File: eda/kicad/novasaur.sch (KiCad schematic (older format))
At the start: 29 parts, among them U1 74F86, U10 74F574, U11 74F574, U12 PAL16R4, U2 74F32, U3 74F11, U4 74F139, U5 74F139, U6 74F157, U7 74F175, U8 74F574, U9 74F138, X1 33M

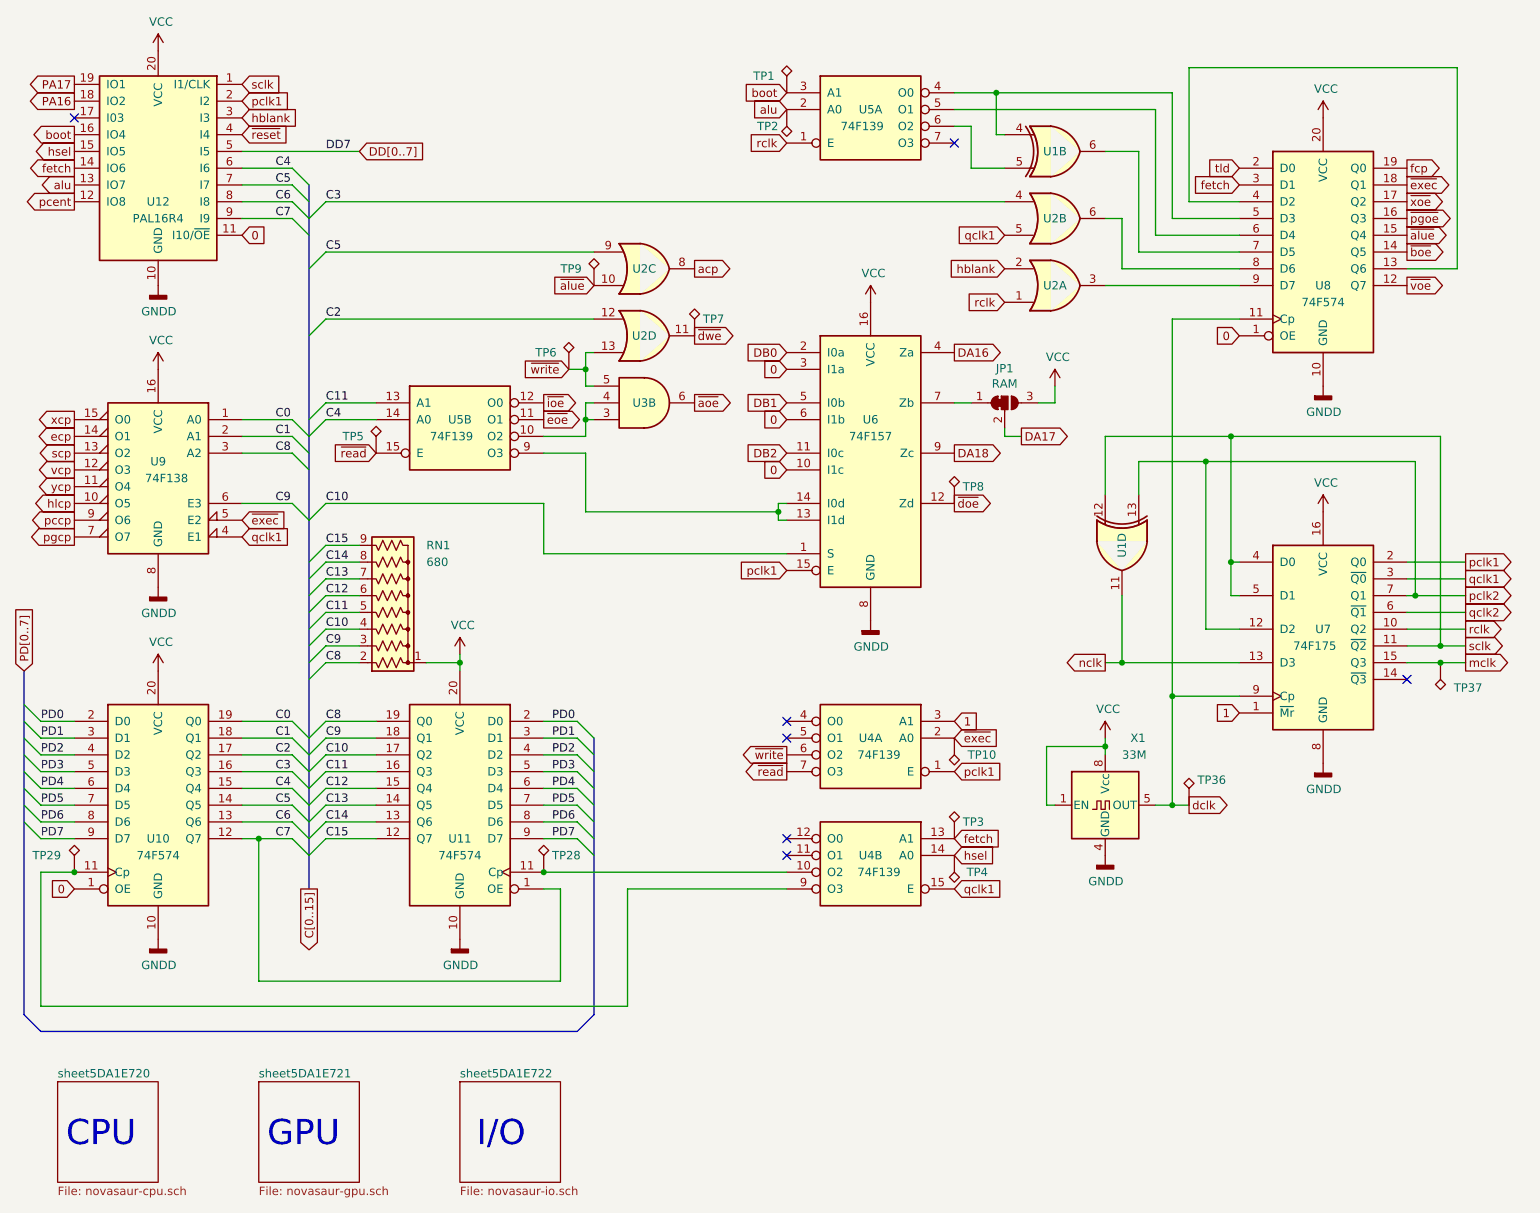
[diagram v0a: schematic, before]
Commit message: add TVS diode ESD protection
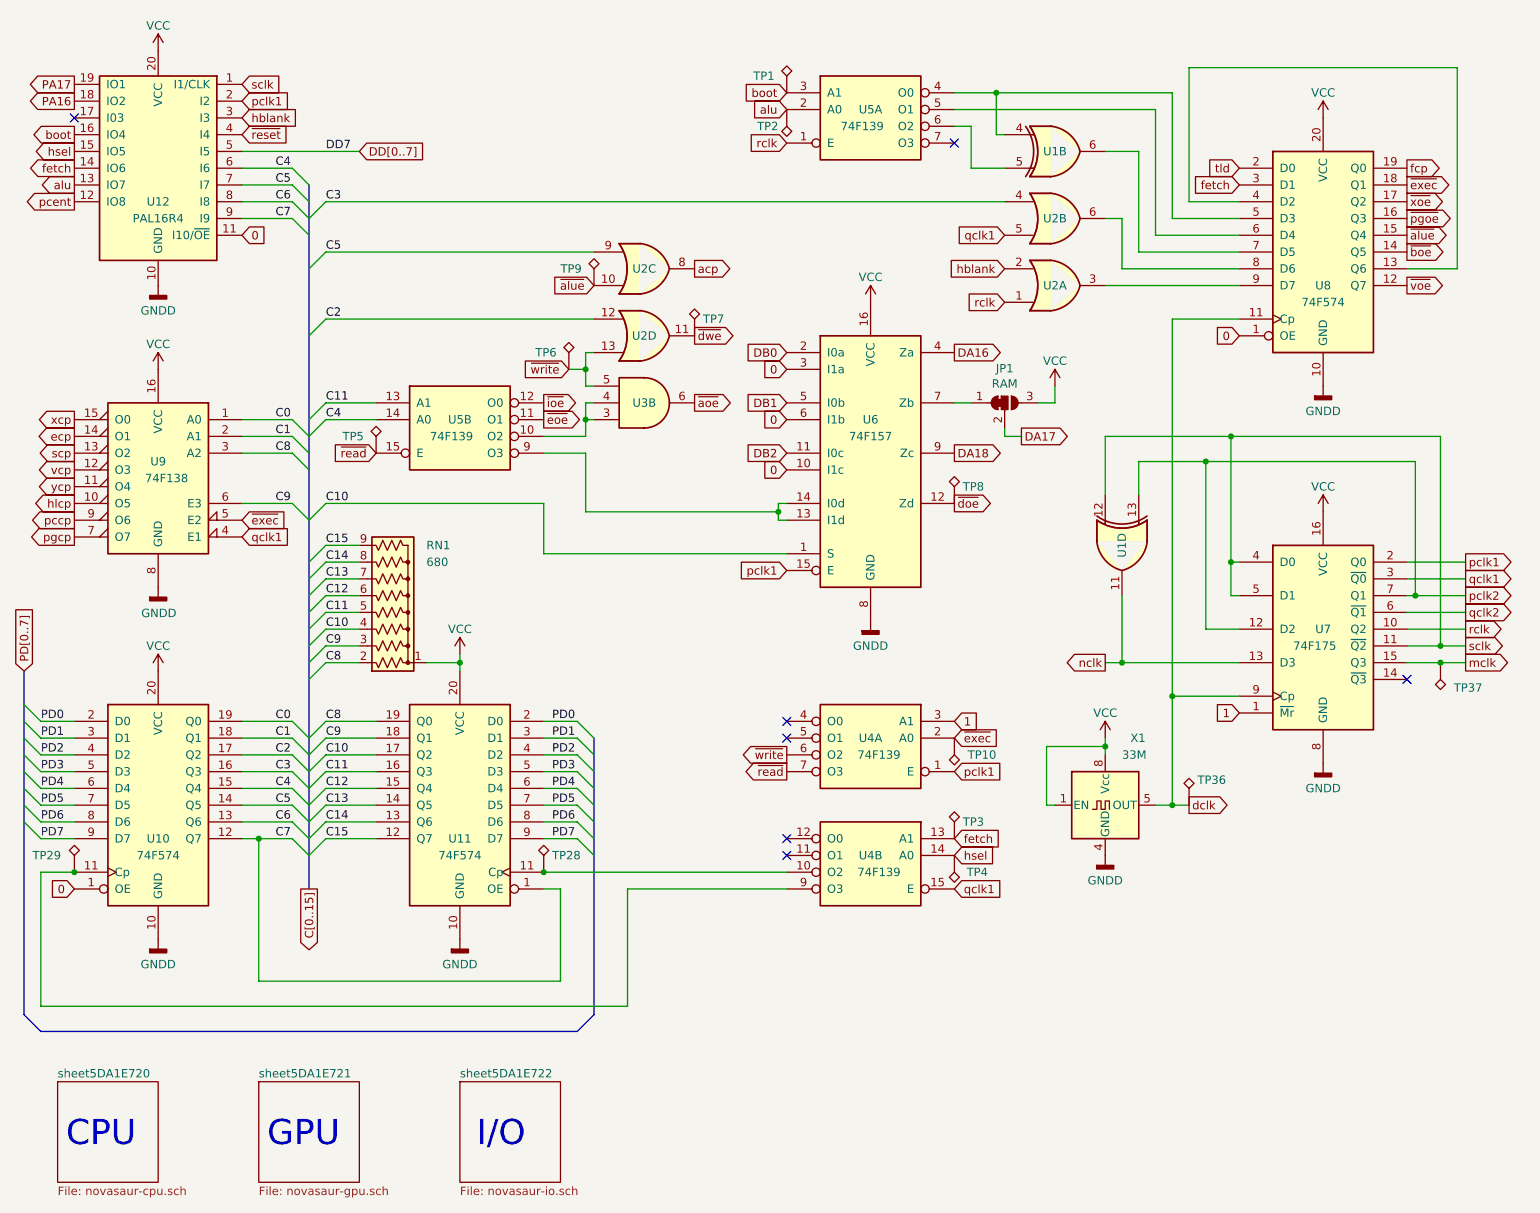
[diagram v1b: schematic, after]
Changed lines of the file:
@@
 Sheet 1 4
 Title "Novasaur Retrocomputer"
-Date "2021-06-06"
-Rev "1.9"
+Date "2021-07-10"
+Rev "1.10"
 Comp ""
 Comment1 "(c) Solid State Machines 2021"
@@
 AR Path="/5DA1E953" Ref="#PWR0114"  Part="1"
 F 0 "#PWR0114" H 1850 6050 50  0001 C CNN
-F 1 "GNDD" H 1854 6145 50  0000 C CNN
+F 1 "GNDD" H 1850 6150 50  0000 C CNN
 F 2 "" H 1850 6300 50  0001 C CNN
 F 3 "" H 1850 6300 50  0001 C CNN
@@
 AR Path="/5DA1E817" Ref="#PWR0110"  Part="1"
 F 0 "#PWR0110" H 1850 2150 50  0001 C CNN
-F 1 "GNDD" H 1854 2245 50  0000 C CNN
+F 1 "GNDD" H 1850 2250 50  0000 C CNN
 F 2 "" H 1850 2400 50  0001 C CNN
 F 3 "" H 1850 2400 50  0001 C CNN
@@
 AR Path="/5DA1E7E3" Ref="#PWR0107"  Part="1"
 F 0 "#PWR0107" H 3650 6050 50  0001 C CNN
-F 1 "GNDD" H 3654 6145 50  0000 C CNN
+F 1 "GNDD" H 3650 6150 50  0000 C CNN
 F 2 "" H 3650 6300 50  0001 C CNN
 F 3 "" H 3650 6300 50  0001 C CNN
@@
 AR Path="/5DA1E785" Ref="#PWR0105"  Part="1"
 F 0 "#PWR0105" H 1850 4550 50  0001 C CNN
-F 1 "VCC" H 1867 4873 50  0000 C CNN
+F 1 "VCC" H 1850 4850 50  0000 C CNN
 F 2 "" H 1850 4700 50  0001 C CNN
 F 3 "" H 1850 4700 50  0001 C CNN
@@
 AR Path="/5DA1E756" Ref="#PWR0104"  Part="1"
 F 0 "#PWR0104" H 1850 2750 50  0001 C CNN
-F 1 "VCC" H 1867 3073 50  0000 C CNN
+F 1 "VCC" H 1850 3050 50  0000 C CNN
 F 2 "" H 1850 2900 50  0001 C CNN
 F 3 "" H 1850 2900 50  0001 C CNN
@@
 AR Path="/5DA1E7F9" Ref="#PWR0108"  Part="1"
 F 0 "#PWR0108" H 3650 4450 50  0001 C CNN
-F 1 "VCC" H 3667 4773 50  0000 C CNN
+F 1 "VCC" H 3650 4750 50  0000 C CNN
 F 2 "" H 3650 4600 50  0001 C CNN
 F 3 "" H 3650 4600 50  0001 C CNN
@@
 AR Path="/5EAB4390" Ref="#PWR0101"  Part="1"
 F 0 "#PWR0101" H 8800 2750 50  0001 C CNN
-F 1 "GNDD" H 8804 2845 50  0000 C CNN
+F 1 "GNDD" H 8800 2850 50  0000 C CNN
 F 2 "" H 8800 3000 50  0001 C CNN
 F 3 "" H 8800 3000 50  0001 C CNN
@@
 AR Path="/5EAB4396" Ref="#PWR0106"  Part="1"
 F 0 "#PWR0106" H 8800 1250 50  0001 C CNN
-F 1 "VCC" H 8817 1573 50  0000 C CNN
+F 1 "VCC" H 8800 1550 50  0000 C CNN
 F 2 "" H 8800 1400 50  0001 C CNN
 F 3 "" H 8800 1400 50  0001 C CNN
@@
 AR Path="/5DE9082F" Ref="#PWR0113"  Part="1"
 F 0 "#PWR0113" H 1850 850 50  0001 C CNN
-F 1 "VCC" H 1867 1173 50  0000 C CNN
+F 1 "VCC" H 1850 1150 50  0000 C CNN
 F 2 "" H 1850 1000 50  0001 C CNN
 F 3 "" H 1850 1000 50  0001 C CNN
@@
 AR Path="/5E57D7F8" Ref="#PWR0192"  Part="1"
 F 0 "#PWR0192" H 6100 2350 50  0001 C CNN
-F 1 "VCC" H 6117 2673 50  0000 C CNN
+F 1 "VCC" H 6100 2650 50  0000 C CNN
 F 2 "" H 6100 2500 50  0001 C CNN
 F 3 "" H 6100 2500 50  0001 C CNN
@@
 AR Path="/5D9CBE89" Ref="#PWR0112"  Part="1"
 F 0 "#PWR0112" H 7500 5550 50  0001 C CNN
-F 1 "GNDD" H 7504 5645 50  0000 C CNN
+F 1 "GNDD" H 7500 5650 50  0000 C CNN
 F 2 "" H 7500 5800 50  0001 C CNN
 F 3 "" H 7500 5800 50  0001 C CNN
@@
 AR Path="/5DAA5CD8/5D9DED2A" Ref="#PWR?"  Part="1"
 F 0 "#PWR0191" H 7500 4950 50  0001 C CNN
-F 1 "VCC" H 7517 5273 50  0000 C CNN
+F 1 "VCC" H 7500 5250 50  0000 C CNN
 F 2 "" H 7500 5100 50  0001 C CNN
 F 3 "" H 7500 5100 50  0001 C CNN
@@
 AR Path="/5DEA197D" Ref="#PWR0103"  Part="1"
 F 0 "#PWR0103" H 8800 5000 50  0001 C CNN
-F 1 "GNDD" H 8804 5095 50  0000 C CNN
+F 1 "GNDD" H 8800 5100 50  0000 C CNN
 F 2 "" H 8800 5250 50  0001 C CNN
 F 3 "" H 8800 5250 50  0001 C CNN
@@
 AR Path="/5DA5D9DA" Ref="#PWR0102"  Part="1"
 F 0 "#PWR0102" H 8800 3600 50  0001 C CNN
-F 1 "VCC" H 8817 3923 50  0000 C CNN
+F 1 "VCC" H 8800 3900 50  0000 C CNN
 F 2 "" H 8800 3750 50  0001 C CNN
 F 3 "" H 8800 3750 50  0001 C CNN
@@
 AR Path="/5E58D7F4" Ref="#PWR0193"  Part="1"
 F 0 "#PWR0193" H 6100 4150 50  0001 C CNN
-F 1 "GNDD" H 6104 4245 50  0000 C CNN
+F 1 "GNDD" H 6100 4250 50  0000 C CNN
 F 2 "" H 6100 4400 50  0001 C CNN
 F 3 "" H 6100 4400 50  0001 C CNN
@@
 AR Path="/5EAF98E7" Ref="#PWR0198"  Part="1"
 F 0 "#PWR0198" H 7200 2850 50  0001 C CNN
-F 1 "VCC" H 7217 3173 50  0000 C CNN
+F 1 "VCC" H 7200 3150 50  0000 C CNN
 F 2 "" H 7200 3000 50  0001 C CNN
 F 3 "" H 7200 3000 50  0001 C CNN

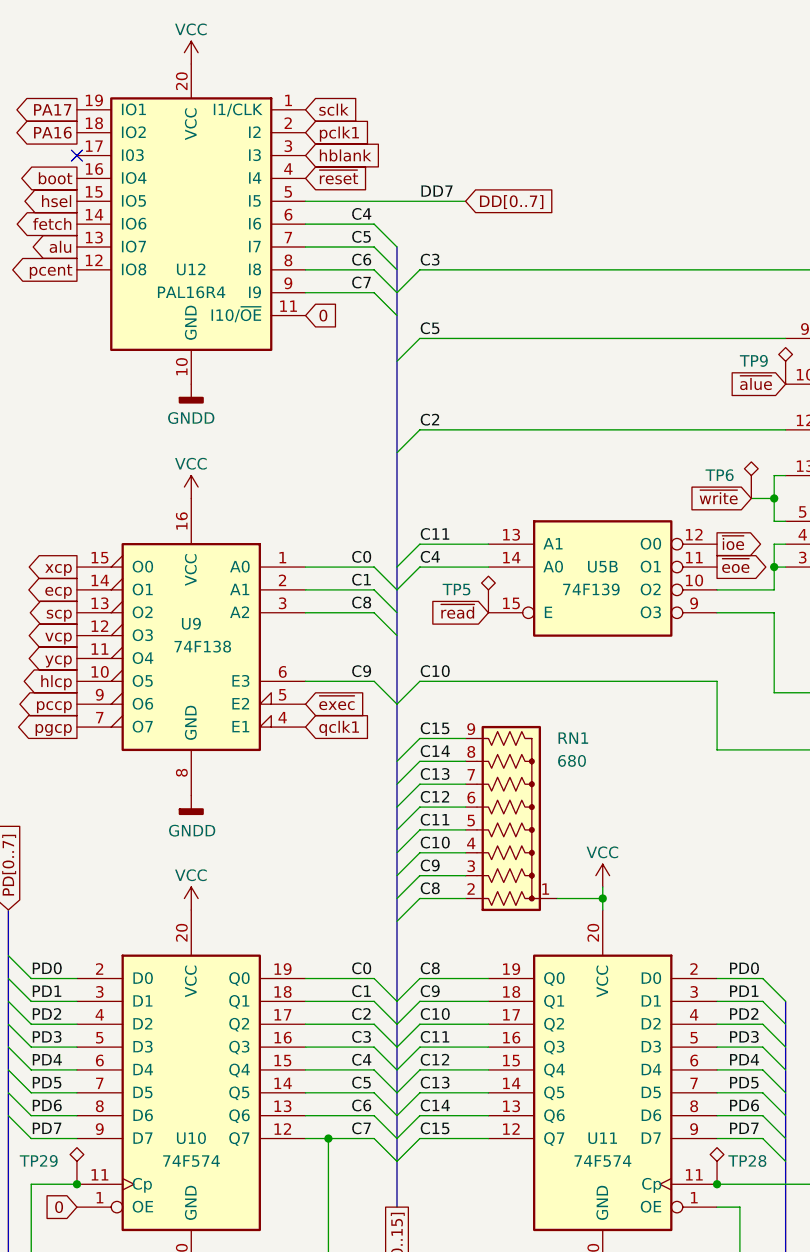
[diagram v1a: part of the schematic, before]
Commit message: remove 6v regulator go back to rev.1 do not collect 00
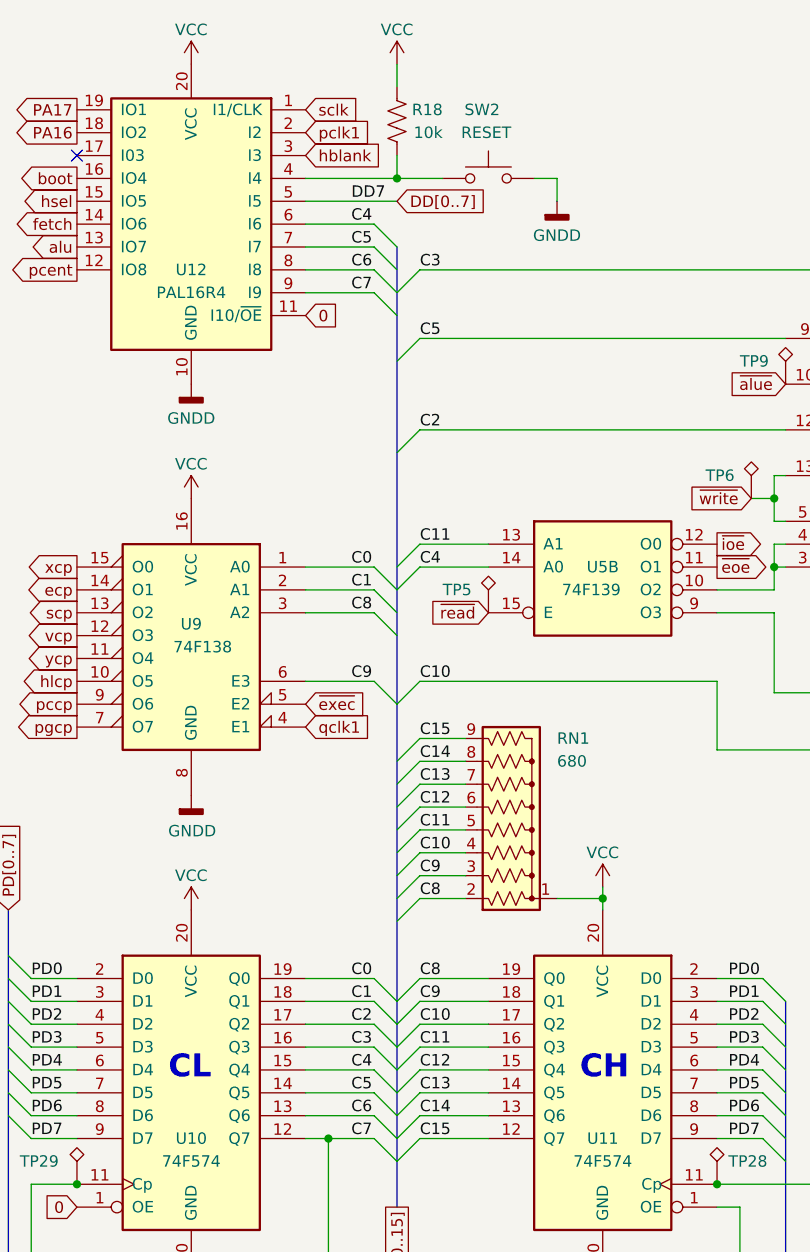
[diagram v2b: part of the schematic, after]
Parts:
- added R18: 10k, Resistor_THT:R_Axial_DIN0204_L3.6mm_D1.6mm_P7.62mm_Horizontal, symbol Device:R_US
- added SW2: RESET, Button_Switch_THT:SW_Tactile_SPST_Angled_PTS645Vx31-2LFS, symbol Switch:SW_Push
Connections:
- net GNDD: now also SW2.1
- net VCC: now also R18.2
- net ~reset: no longer names the net of U12.4 (I4)
- net ~reset: now also R18.1, SW2.2
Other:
- note added: "CH"
- note added: "CL"
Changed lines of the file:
@@
 Sheet 1 4
 Title "Novasaur Retrocomputer"
-Date "2021-07-10"
+Date "2021-08-01"
 Rev "1.10"
 Comp ""
@@
 	5600 5900 4150 5900
 Connection ~ 4150 5900
-Text GLabel 2350 1500 2    50   Input ~ 0
-~reset
 $Comp
 L Connector:TestPoint_Alt TP28
@@
 Wire Wire Line
 	9500 4650 9650 4650
-Wire Wire Line
-	2350 1600 3050 1600
-Text Label 2850 1600 0    50   ~ 0
+Text Label 2550 1600 0    50   ~ 0
 DD7
-Text GLabel 3050 1600 2    50   Input ~ 0
+Text GLabel 2750 1600 2    50   Input ~ 0
 DD[0..7]
 $Comp
@@
 Wire Wire Line
 	4150 4000 5600 4000
+Text Notes 1750 5450 0    100  ~ 20
+CL
+Text Notes 3550 5450 0    100  ~ 20
+CH
+$Comp
+L Device:R_US R?
+U 1 1 6116EADB
+P 2750 1250
+AR Path="/62D13D9D/6116EADB" Ref="R?"  Part="1"
+AR Path="/5DAA5CD8/5D9AFF37/6116EADB" Ref="R?"  Part="1"
+AR Path="/5DA1E9C0/6116EADB" Ref="R?"  Part="1"
+AR Path="/6116EADB" Ref="R18"  Part="1"
+F 0 "R18" H 2550 1200 50  0000 L CNN
+F 1 "10k" H 2550 1300 50  0000 L CNN
+F 2 "Resistor_THT:R_Axial_DIN0204_L3.6mm_D1.6mm_P7.62mm_Horizontal" V 2790 1240 50  0001 C CNN
+F 3 "~" H 2750 1250 50  0001 C CNN
+	1    2750 1250
+	-1   0    0    1
+$EndComp
+$Comp
+L Switch:SW_Push SW?
+U 1 1 6116EAE1
+P 3150 1500
+AR Path="/5DA1E9C0/6116EAE1" Ref="SW?"  Part="1"
+AR Path="/6116EAE1" Ref="SW2"  Part="1"
+F 0 "SW2" H 3100 1800 50  0000 L CNN
+F 1 "RESET" H 3050 1700 50  0000 L CNN
+F 2 "Button_Switch_THT:SW_Tactile_SPST_Angled_PTS645Vx31-2LFS" H 3150 1700 50  0001 C CNN
+F 3 "~" H 3150 1700 50  0001 C CNN
+	1    3150 1500
+	-1   0    0    -1
+$EndComp
+$Comp
+L power:VCC #PWR?
+U 1 1 611A0A05
+P 2750 1000
+AR Path="/5CDEEC9F/611A0A05" Ref="#PWR?"  Part="1"
+AR Path="/5DAA5CD8/611A0A05" Ref="#PWR?"  Part="1"
+AR Path="/611A0A05" Ref="#PWR0197"  Part="1"
+F 0 "#PWR0197" H 2750 850 50  0001 C CNN
+F 1 "VCC" H 2750 1150 50  0000 C CNN
+F 2 "" H 2750 1000 50  0001 C CNN
+F 3 "" H 2750 1000 50  0001 C CNN
+	1    2750 1000
+	1    0    0    -1
+$EndComp
+Wire Wire Line
+	2750 1100 2750 1000
+Wire Wire Line
+	2350 1500 2750 1500
+Wire Wire Line
+	2750 1500 2750 1400
+Connection ~ 2750 1500
+Wire Wire Line
+	2750 1500 2950 1500
+Wire Wire Line
+	3350 1500 3450 1500
+Wire Wire Line
+	3450 1500 3450 1600
+$Comp
+L power:GNDD #PWR?
+U 1 1 611D649A
+P 3450 1600
+AR Path="/5CDEEC9F/611D649A" Ref="#PWR?"  Part="1"
+AR Path="/5DAA5CD8/611D649A" Ref="#PWR?"  Part="1"
+AR Path="/611D649A" Ref="#PWR0199"  Part="1"
+F 0 "#PWR0199" H 3450 1350 50  0001 C CNN
+F 1 "GNDD" H 3450 1450 50  0000 C CNN
+F 2 "" H 3450 1600 50  0001 C CNN
+F 3 "" H 3450 1600 50  0001 C CNN
+	1    3450 1600
+	1    0    0    -1
+$EndComp
+Wire Wire Line
+	2750 1600 2350 1600
 Wire Bus Line
 	4450 5100 4450 6750

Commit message: Rev. 10 with 5v PSU
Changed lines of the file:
@@
 Sheet 1 4
 Title "Novasaur Retrocomputer"
-Date "2021-08-01"
+Date "2021-09-02"
 Rev "1.10"
 Comp ""
@@
 Wire Wire Line
 	4150 4000 5600 4000
-Text Notes 1750 5450 0    100  ~ 20
+Text Notes 1750 5450 0    100  ~ 0
 CL
-Text Notes 3550 5450 0    100  ~ 20
+Text Notes 3550 5450 0    100  ~ 0
 CH
 $Comp
